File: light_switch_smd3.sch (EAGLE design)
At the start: 19 parts

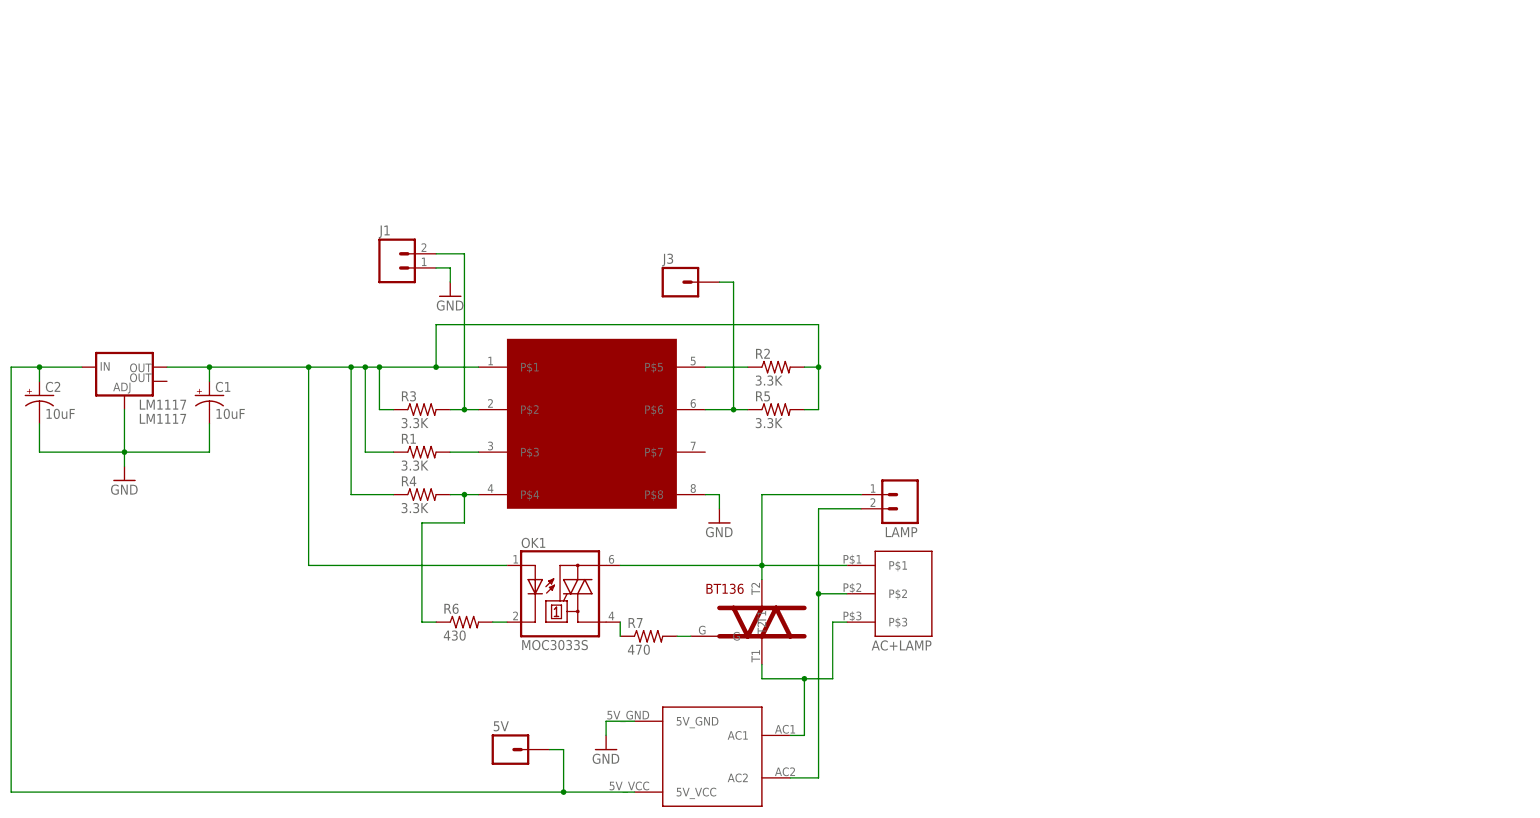
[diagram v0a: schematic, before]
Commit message: major update. added second relay circuit, redesigned board
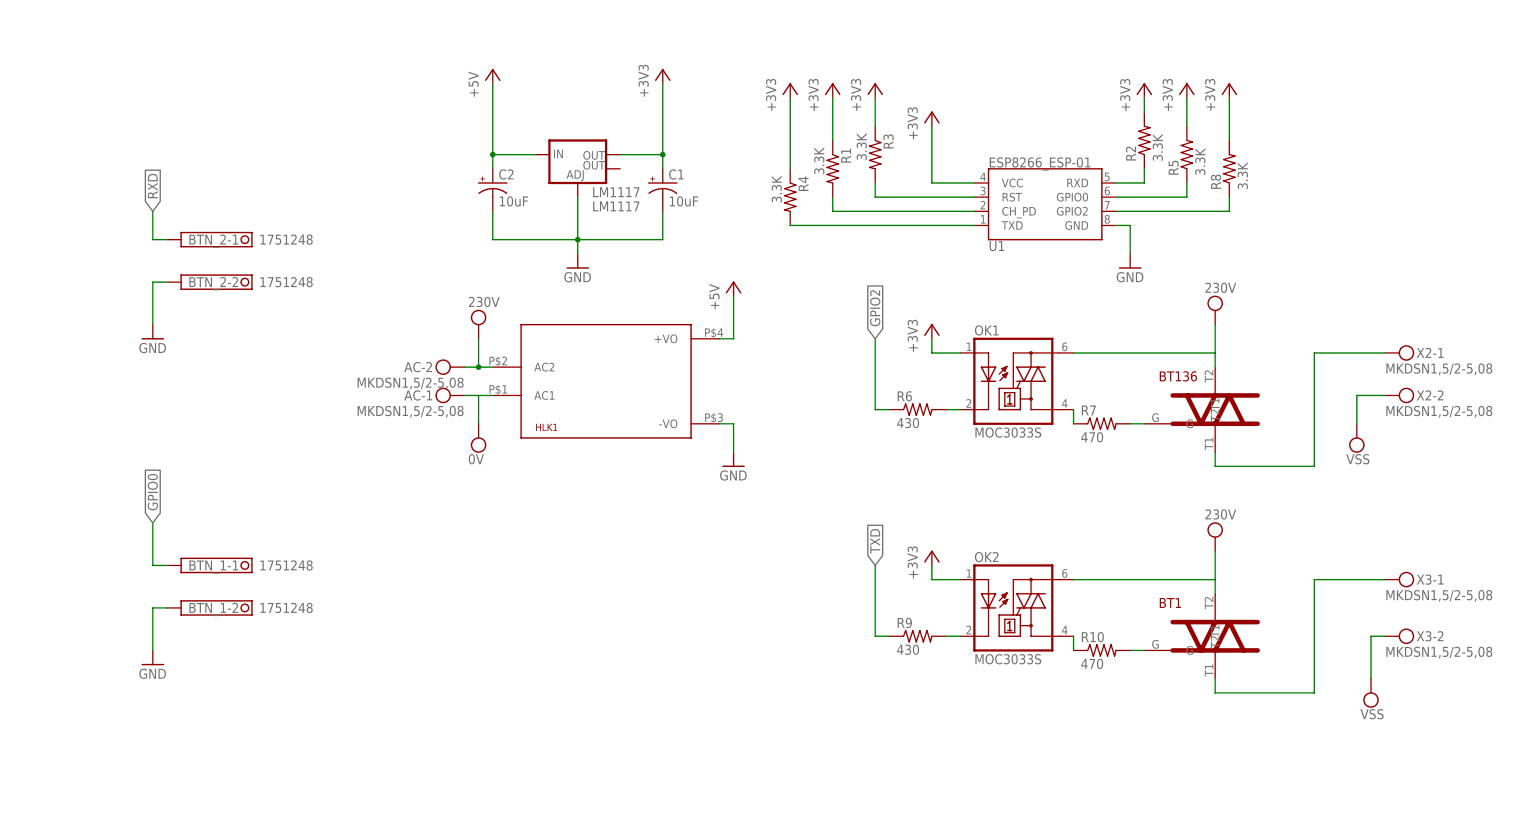
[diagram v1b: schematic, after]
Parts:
- removed 5V, J3: (no value), SparkFun-Connectors:M01PTH
- removed AC+LAMP: DG350-3.5-03P, myblog_library:DG350-3.5-03P
- removed J1, LAMP: (no value), SparkFun-Connectors:M02PTH
- removed U$1: HI-LINK5V-ACDC, myblog_library:HI-LINK5V-ACDC
- removed U$2: ESP8266-01, myblog_library:ESP8266-01
- added AC, X2, X3: MKDSN1,5/2-5,08, con-phoenix-508:MKDSN1,5/2-5,08
- added BT1: BT136, myblog_library:BT136
- added BTN_1, BTN_2: 1751248, con-phoenix-350:1751248
- added HLK1: HLK-PM013W, HLK-PM01:HLK-PM013W
- added OK2: MOC3033S, optocoupler:MOC3033S
- added R10: 470, SparkFun-Resistors:RESISTOR0603
- added R8: 3.3K, SparkFun-Resistors:3.3MOHM-1/10W-1%(0603)
- added R9: 430, SparkFun-Resistors:RESISTOR0603
- added U1: ESP8266_ESP-01, SparkFun-RF:ESP8266_ESP-01
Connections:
- removed net N$11: AC+LAMP.P$2, LAMP.2, U$1.AC2
- removed net N$12: AC+LAMP.P$3, BT136.T1, U$1.AC1
- new net +3V3: C1.+, LM1117.OUT, OK1.A, OK2.A, R2.2, R3.1, R8.2, U1.VCC
- new net +5V: C2.+, HLK1.+VO, LM1117.IN
- new net GPIO0: BTN_1-1.K, R5.1, U1.GPIO0
- new net GPIO2: R6.1, R8.1, U1.GPIO2
- new net N$27: R4.1
- new net N$28: R5.2
- new net N$4: BT136.T1, X2-1.KL
- new net RXD: BTN_2-1.K, R2.1, U1.RXD
- new net TXD: R9.1
- new net VPP: AC-2.KL, BT1.T2, BT136.T2, HLK1.AC2, OK1.A2, OK2.A2
- new net VSS: AC-1.KL, HLK1.AC1, X2-2.KL, X3-2.KL
- net GND: now also BTN_1-2.K, BTN_2-2.K, HLK1.-VO, U1.GND; no longer J1.1, U$1.5V_GND, U$2.P$8
- net N$1: now also U1.RST; no longer J1.2, U$2.P$2
- net N$13: now also R1.1; no longer 5V.1, C2.+, LM1117.IN, U$1.5V_VCC
- net N$14: now also BT1.G, R10.2; no longer J3.1, R5.1, U$2.P$6
- net N$2: now also OK2.C, R9.2; no longer R2.1, U$2.P$5
- net N$26: now also U1.CH_PD; no longer U$2.P$3
- net N$3: now also OK2.A1, R10.1; no longer C1.+, LM1117.OUT, OK1.A, R1.1, R2.2, R3.1, R4.1, R5.2, U$2.P$1
- net N$8: now also BT1.T1, X3-1.KL; no longer AC+LAMP.P$1, BT136.T2, LAMP.1, OK1.A2
- net N$9: now also U1.TXD; no longer R6.1, U$2.P$4
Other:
- moved on the sheet: BT136, C1, C2, LM1117, OK1, R1, R2, R3, R4, R5, R6, R7

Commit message: almost ready for production. some descriptions needs adjusting.
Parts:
- added R11: 3.3K, SparkFun-Resistors:3.3MOHM-1/10W-1%(0603)
- added SENSOR: (no value), pinhead:PINHD-1X3
- renumbered X2 to OUT_1, X3 to OUT_2
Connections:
- net N$1 renamed RST
- net N$26 renamed CH_PD
- removed net N$9: R4.2, U1.TXD
- new net DATA: R11.2, SENSOR.2
- net +3V3: now also R11.1, SENSOR.3
- net GND: now also SENSOR.1
- net TXD: now also R4.2, U1.TXD

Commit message: minor bugs fixed
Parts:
- R11: value 3.3K -> 4.7K
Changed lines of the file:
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@@
 <part name="GND6" library="supply1" deviceset="GND" device=""/>
 <part name="+3V11" library="supply1" deviceset="+3V3" device=""/>
-<part name="R11" library="SparkFun-Resistors" deviceset="3.3MOHM-1/10W-1%(0603)" device="" value="3.3K"/>
+<part name="R11" library="SparkFun-Resistors" deviceset="3.3MOHM-1/10W-1%(0603)" device="" value="4.7K"/>
 <part name="+3V12" library="supply1" deviceset="+3V3" device=""/>
 </parts>

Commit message: sligthly bigger smd parts, for easier soldering
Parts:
- C1, C2: device SparkFun-Capacitors:10UF-6.3V-20%(0603)(TANT)" -> resistor:CPOL-USA/3216-18R
- R1, R11, R2, R3, R4, R5, R8: device SparkFun-Resistors:3.3MOHM-1/10W-1%(0603) -> resistor:R-US_R1206
- R10, R6, R7, R9: device SparkFun-Resistors:RESISTOR0603 -> resistor:R-US_R1206
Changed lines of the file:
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@@
 <parts>
 <part name="LM1117" library="SparkFun-PowerIC" deviceset="V_REG_LM1117" device="SOT223" value="LM1117"/>
-<part name="C1" library="SparkFun-Capacitors" deviceset="10UF-6.3V-20%(0603)(TANT)" device="&quot;" value="10uF"/>
-<part name="C2" library="SparkFun-Capacitors" deviceset="10UF-6.3V-20%(0603)(TANT)" device="&quot;" value="10uF"/>
-<part name="R1" library="SparkFun-Resistors" deviceset="3.3MOHM-1/10W-1%(0603)" device="" value="3.3K"/>
-<part name="R2" library="SparkFun-Resistors" deviceset="3.3MOHM-1/10W-1%(0603)" device="" value="3.3K"/>
-<part name="R3" library="SparkFun-Resistors" deviceset="3.3MOHM-1/10W-1%(0603)" device="" value="3.3K"/>
-<part name="R4" library="SparkFun-Resistors" deviceset="3.3MOHM-1/10W-1%(0603)" device="" value="3.3K"/>
-<part name="R5" library="SparkFun-Resistors" deviceset="3.3MOHM-1/10W-1%(0603)" device="" value="3.3K"/>
-<part name="R6" library="SparkFun-Resistors" deviceset="RESISTOR" device="0603" value="430"/>
-<part name="R7" library="SparkFun-Resistors" deviceset="RESISTOR" device="0603" value="470"/>
+<part name="C1" library="resistor" deviceset="CPOL-US" device="A/3216-18R" value="10uF"/>
+<part name="C2" library="resistor" deviceset="CPOL-US" device="A/3216-18R" value="10uF"/>
+<part name="R1" library="resistor" deviceset="R-US_" device="R1206" value="3.3K"/>
+<part name="R2" library="resistor" deviceset="R-US_" device="R1206" value="3.3K"/>
+<part name="R3" library="resistor" deviceset="R-US_" device="R1206" value="3.3K"/>
+<part name="R4" library="resistor" deviceset="R-US_" device="R1206" value="3.3K"/>
+<part name="R5" library="resistor" deviceset="R-US_" device="R1206" value="3.3K"/>
+<part name="R6" library="resistor" deviceset="R-US_" device="R1206" value="430"/>
+<part name="R7" library="resistor" deviceset="R-US_" device="R1206" value="470"/>
 <part name="GND1" library="supply1" deviceset="GND" device=""/>
 <part name="GND2" library="supply1" deviceset="GND" device=""/>
@@
 <part name="+3V3" library="supply1" deviceset="+3V3" device=""/>
 <part name="+3V4" library="supply1" deviceset="+3V3" device=""/>
-<part name="R8" library="SparkFun-Resistors" deviceset="3.3MOHM-1/10W-1%(0603)" device="" value="3.3K"/>
+<part name="R8" library="resistor" deviceset="R-US_" device="R1206" value="3.3K"/>
 <part name="SUPPLY1" library="supply2" deviceset="VPP" device="" value="230V"/>
 <part name="SUPPLY2" library="supply2" deviceset="VSS" device="" value="0V"/>
@@
 <part name="GND4" library="supply1" deviceset="GND" device=""/>
 <part name="GND5" library="supply1" deviceset="GND" device=""/>
-<part name="R9" library="SparkFun-Resistors" deviceset="RESISTOR" device="0603" value="430"/>
-<part name="R10" library="SparkFun-Resistors" deviceset="RESISTOR" device="0603" value="470"/>
+<part name="R9" library="resistor" deviceset="R-US_" device="R1206" value="430"/>
+<part name="R10" library="resistor" deviceset="R-US_" device="R1206" value="470"/>
 <part name="OK2" library="optocoupler" deviceset="MOC30*" device="S" technology="33"/>
 <part name="BT1" library="myblog_library" deviceset="BT136" device=""/>
@@
 <part name="GND6" library="supply1" deviceset="GND" device=""/>
 <part name="+3V11" library="supply1" deviceset="+3V3" device=""/>
-<part name="R11" library="SparkFun-Resistors" deviceset="3.3MOHM-1/10W-1%(0603)" device="" value="4.7K"/>
+<part name="R11" library="resistor" deviceset="R-US_" device="R1206" value="4.7K"/>
 <part name="+3V12" library="supply1" deviceset="+3V3" device=""/>
 </parts>
@@
 <instance part="C1" gate="G$1" x="101.6" y="106.68" smashed="yes">
 <attribute name="NAME" x="102.616" y="107.315" size="1.778" layer="95"/>
-<attribute name="VALUE" x="102.616" y="102.489" size="1.778" layer="96"/>
 </instance>
 <instance part="C2" gate="G$1" x="71.12" y="106.68" smashed="yes">
 <attribute name="NAME" x="72.136" y="107.315" size="1.778" layer="95"/>
-<attribute name="VALUE" x="72.136" y="102.489" size="1.778" layer="96"/>
 </instance>
 <instance part="R1" gate="G$1" x="132.08" y="109.22" smashed="yes" rot="R270">

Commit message: added missing sensor data connection
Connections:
- removed net DATA: R11.2, SENSOR.2
- net RXD: now also R11.2, SENSOR.2
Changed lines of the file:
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@@
 <label x="10.16" y="101.6" size="1.778" layer="95" rot="R90" xref="yes"/>
+</segment>
+<segment>
+<pinref part="SENSOR" gate="A" pin="2"/>
+<pinref part="R11" gate="G$1" pin="2"/>
+<wire x1="68.58" y1="30.48" x2="91.44" y2="30.48" width="0.1524" layer="91"/>
+<wire x1="91.44" y1="30.48" x2="101.6" y2="30.48" width="0.1524" layer="91"/>
+<wire x1="101.6" y1="30.48" x2="101.6" y2="35.56" width="0.1524" layer="91"/>
+<junction x="91.44" y="30.48"/>
+<label x="101.6" y="38.1" size="1.778" layer="95" rot="R90"/>
 </segment>
 </net>
@@
 </segment>
 </net>
-<net name="DATA" class="0">
-<segment>
-<pinref part="SENSOR" gate="A" pin="2"/>
-<pinref part="R11" gate="G$1" pin="2"/>
-<wire x1="68.58" y1="30.48" x2="91.44" y2="30.48" width="0.1524" layer="91"/>
-</segment>
-</net>

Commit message: small fixes to be more ERC friendly
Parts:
- SENSOR: value (none) -> CON1
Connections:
- removed net N$13: R1.1
- removed net N$27: R4.1
- removed net N$28: R5.2
- net +3V3: now also R1.1, R4.1, R5.2
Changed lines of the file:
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@@
 <part name="+3V10" library="supply1" deviceset="+3V3" device=""/>
 <part name="SUPPLY6" library="supply2" deviceset="VSS" device=""/>
-<part name="SENSOR" library="pinhead" deviceset="PINHD-1X3" device=""/>
+<part name="SENSOR" library="pinhead" deviceset="PINHD-1X3" device="" value="CON1"/>
 <part name="GND6" library="supply1" deviceset="GND" device=""/>
 <part name="+3V11" library="supply1" deviceset="+3V3" device=""/>
@@
 <wire x1="195.58" y1="106.68" x2="195.58" y2="104.14" width="0.1524" layer="91"/>
 <wire x1="195.58" y1="104.14" x2="182.88" y2="104.14" width="0.1524" layer="91"/>
+<label x="187.96" y="104.14" size="1.778" layer="95"/>
 </segment>
 <segment>
@@
 <pinref part="U1" gate="G$1" pin="RXD"/>
 <wire x1="187.96" y1="106.68" x2="182.88" y2="106.68" width="0.1524" layer="91"/>
+<label x="182.88" y="106.68" size="1.778" layer="95"/>
 </segment>
 <segment>
@@
 <wire x1="101.6" y1="30.48" x2="101.6" y2="35.56" width="0.1524" layer="91"/>
 <junction x="91.44" y="30.48"/>
-<label x="101.6" y="38.1" size="1.778" layer="95" rot="R90"/>
+<label x="101.6" y="35.56" size="1.778" layer="95" rot="R90" xref="yes"/>
 </segment>
 </net>
@@
 <wire x1="91.44" y1="40.64" x2="91.44" y2="45.72" width="0.1524" layer="91"/>
 </segment>
+<segment>
+<pinref part="R1" gate="G$1" pin="1"/>
+<wire x1="132.08" y1="114.3" x2="132.08" y2="121.92" width="0.1524" layer="91"/>
+<pinref part="+3V7" gate="G$1" pin="+3V3"/>
+</segment>
+<segment>
+<pinref part="R4" gate="G$1" pin="1"/>
+<wire x1="124.46" y1="109.22" x2="124.46" y2="121.92" width="0.1524" layer="91"/>
+<pinref part="+3V6" gate="G$1" pin="+3V3"/>
+</segment>
+<segment>
+<pinref part="R5" gate="G$1" pin="2"/>
+<wire x1="195.58" y1="116.84" x2="195.58" y2="121.92" width="0.1524" layer="91"/>
+<pinref part="+3V3" gate="G$1" pin="+3V3"/>
+</segment>
 </net>
 <net name="+5V" class="0">
@@
 </segment>
 </net>
-<net name="N$28" class="0">
-<segment>
-<pinref part="R5" gate="G$1" pin="2"/>
-<wire x1="195.58" y1="116.84" x2="195.58" y2="121.92" width="0.1524" layer="91"/>
-<pinref part="+3V3" gate="G$1" pin="+3V3"/>
-</segment>
-</net>
 <net name="GPIO2" class="0">
 <segment>
@@
 <wire x1="182.88" y1="101.6" x2="203.2" y2="101.6" width="0.1524" layer="91"/>
 <wire x1="203.2" y1="101.6" x2="203.2" y2="104.14" width="0.1524" layer="91"/>
+<label x="193.04" y="101.6" size="1.778" layer="95"/>
 </segment>
 <segment>
@@
 <pinref part="SUPPLY4" gate="G$1" pin="VPP"/>
 <wire x1="200.66" y1="81.28" x2="200.66" y2="76.2" width="0.1524" layer="91"/>
+<junction x="200.66" y="76.2"/>
 </segment>
 <segment>
@@
 <pinref part="SUPPLY5" gate="G$1" pin="VPP"/>
 <wire x1="200.66" y1="40.64" x2="200.66" y2="35.56" width="0.1524" layer="91"/>
+<junction x="200.66" y="35.56"/>
 </segment>
 </net>
@@
 <wire x1="68.58" y1="68.58" x2="71.12" y2="68.58" width="0.1524" layer="91"/>
 <wire x1="68.58" y1="63.5" x2="68.58" y2="68.58" width="0.1524" layer="91"/>
+<junction x="68.58" y="68.58"/>
 </segment>
 <segment>
@@
 </segment>
 </net>
-<net name="N$13" class="0">
-<segment>
-<pinref part="R1" gate="G$1" pin="1"/>
-<wire x1="132.08" y1="114.3" x2="132.08" y2="121.92" width="0.1524" layer="91"/>
-<pinref part="+3V7" gate="G$1" pin="+3V3"/>
-</segment>
-</net>
-<net name="N$27" class="0">
-<segment>
-<pinref part="R4" gate="G$1" pin="1"/>
-<wire x1="124.46" y1="109.22" x2="124.46" y2="121.92" width="0.1524" layer="91"/>
-<pinref part="+3V6" gate="G$1" pin="+3V3"/>
-</segment>
-</net>
 <net name="N$2" class="0">
 <segment>
@@
 <pinref part="U1" gate="G$1" pin="TXD"/>
 <wire x1="124.46" y1="99.06" x2="157.48" y2="99.06" width="0.1524" layer="91"/>
-</segment>
-</net>
+<label x="127" y="99.06" size="1.778" layer="95"/>
+</segment>
+</net>
